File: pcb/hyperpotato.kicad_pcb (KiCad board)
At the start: 2 copper layers, 119.4 x 94.3 mm, 13 parts, among them SW1 SW_Push_45deg, SW10 SW_Push_45deg, SW11 SW_Push_45deg, SW12 SW_Push_45deg, SW13 SW_Push_45deg, SW2 SW_Push_45deg, SW3 SW_Push_45deg, SW4 SW_Push_45deg, SW5 SW_Push_45deg, SW6 SW_Push_45deg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

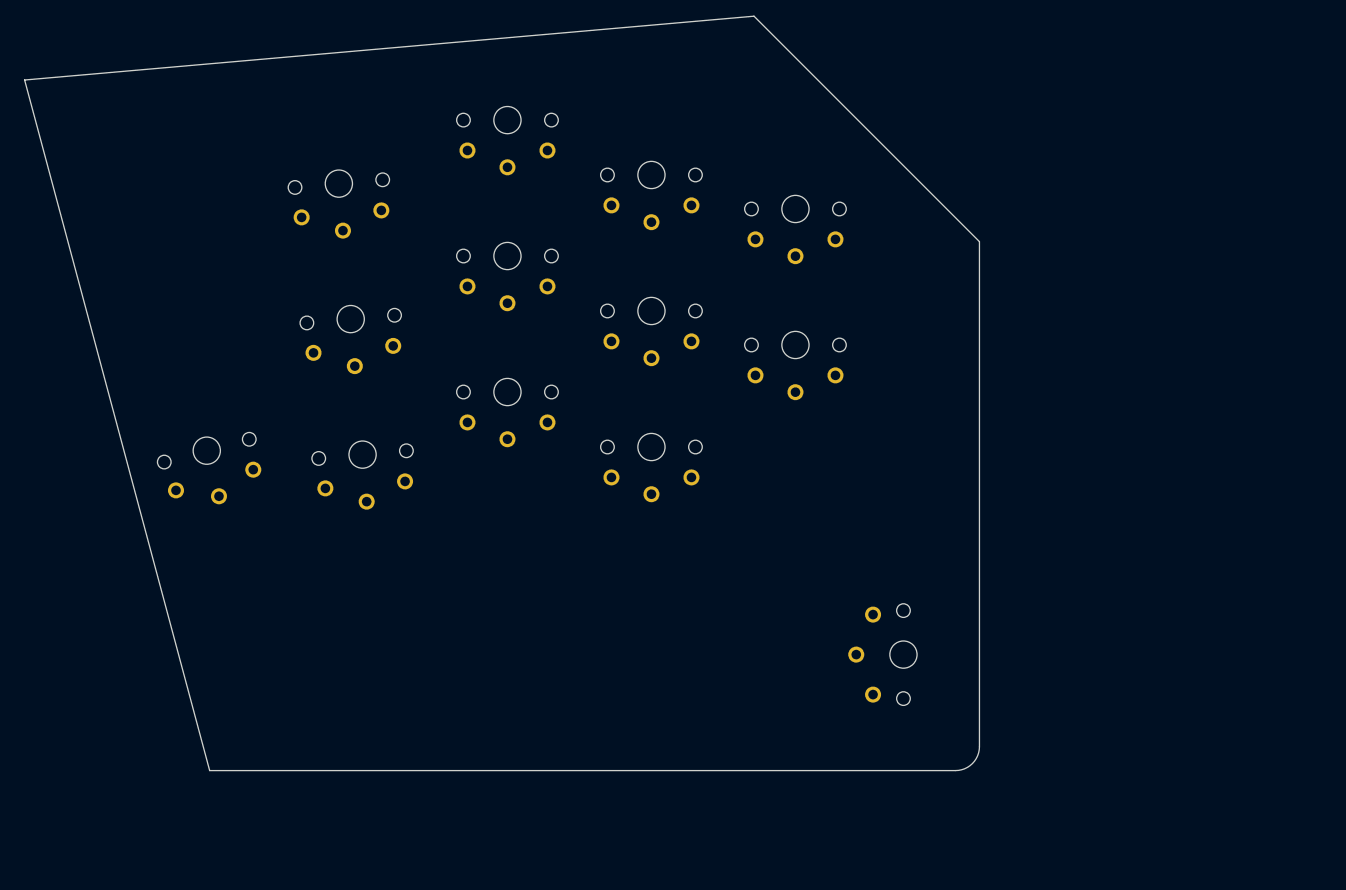
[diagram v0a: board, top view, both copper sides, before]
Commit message: Add pcb outline
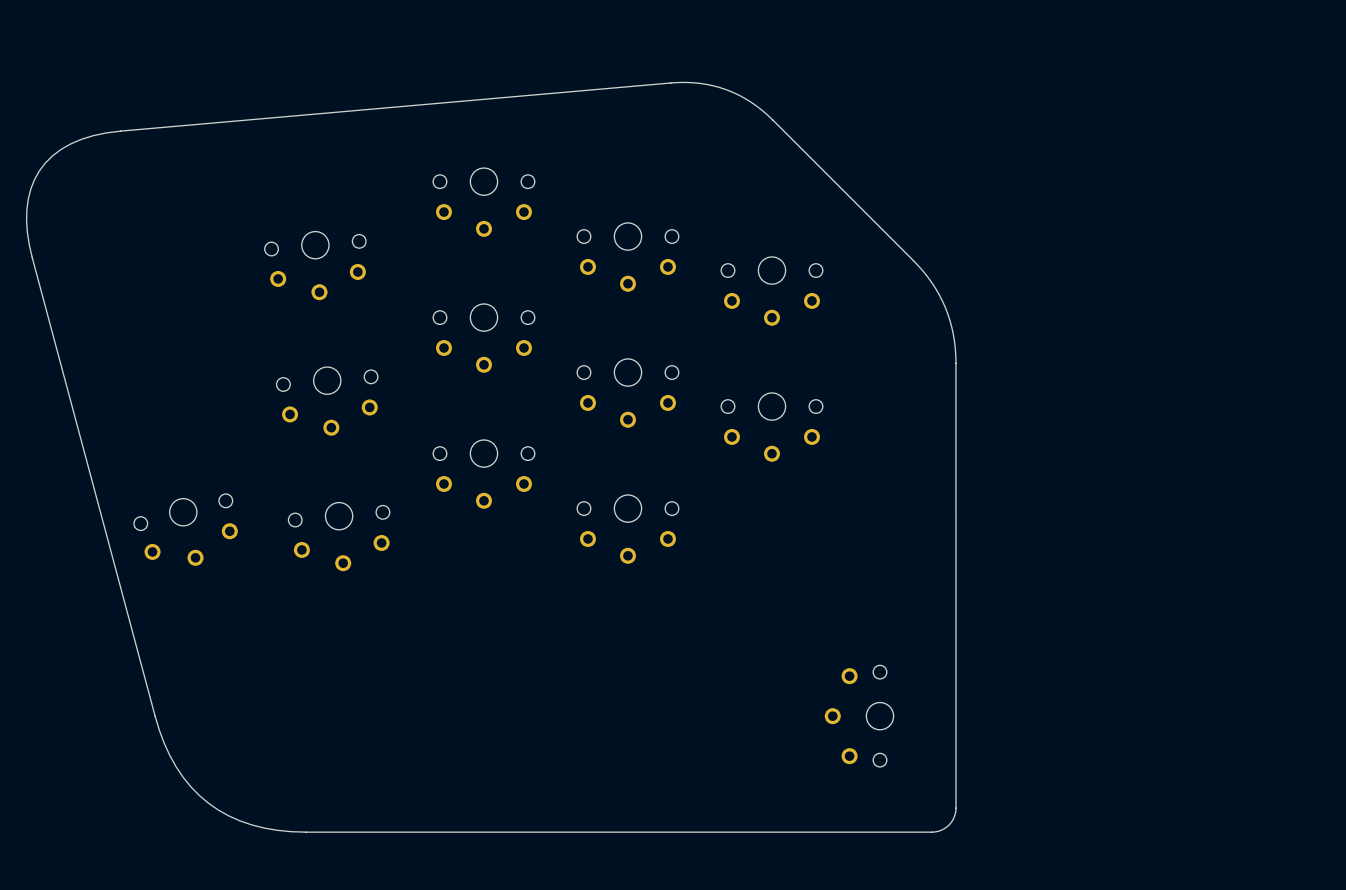
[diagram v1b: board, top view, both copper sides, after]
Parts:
- moved SW9 8.24 mm to (132.6, 91.7)
- moved SW12 8.24 mm to (114.6, 104.5)
- moved SW1 8.24 mm to (75.5, 71.5)
- moved SW10 8.24 mm to (78.4, 105.4)
- moved SW7 8.24 mm to (96.6, 80.6)
- moved SW2 8.24 mm to (96.6, 63.6)
- moved SW13 8.24 mm to (146.1, 130.4)
- moved SW11 8.24 mm to (96.6, 97.6)
- moved SW6 8.24 mm to (77.0, 88.5)
- moved SW4 8.24 mm to (132.6, 74.7)
- moved SW5 8.24 mm to (59.0, 104.9)
- moved SW8 8.24 mm to (114.6, 87.5)
- moved SW3 8.24 mm to (114.6, 70.5)
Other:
- board size 119.4 x 94.3 mm -> 116.2 x 93.7 mm
- board text added: "15mm offset"
- board text added: "3mm offset"
- board text added: "7.5mm offset"

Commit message: Place test xiao footprint
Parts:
- added REF**: Xiao_nRF52840_ACH_1, PCM_marbastlib-xp-promicroish:Xiao_nRF52840_AC_Reflow, F.Cu at (57.3, 64.5)
- moved SW13 5.52 mm to (143.1, 135.1), turned to -95 degrees
- moved SW4 4.20 mm to (134.5, 78.4), turned to -5 degrees
- moved SW9 3.68 mm to (133.0, 95.4), turned to -5 degrees
- moved SW3 3.23 mm to (117.0, 72.6), turned to -5 degrees
- moved SW2 3.13 mm to (99.6, 64.2), turned to -5 degrees
- moved SW5 2.84 mm to (58.6, 102.1), turned to 10 degrees
- moved SW1 2.76 mm to (77.9, 70.3), turned to 0 degrees
- moved SW8 2.29 mm to (115.5, 89.6), turned to -5 degrees
- moved SW12 2.10 mm to (114.0, 106.5), turned to -5 degrees
- moved SW7 1.68 mm to (98.2, 81.2), turned to -5 degrees
- moved SW6 1.54 mm to (77.9, 87.3), turned to 0 degrees
- moved SW10 1.23 mm to (77.9, 104.3), turned to 0 degrees
- moved SW11 0.50 mm to (96.7, 98.1), turned to -5 degrees
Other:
- board size 116.2 x 93.7 mm -> 114.3 x 96.1 mm

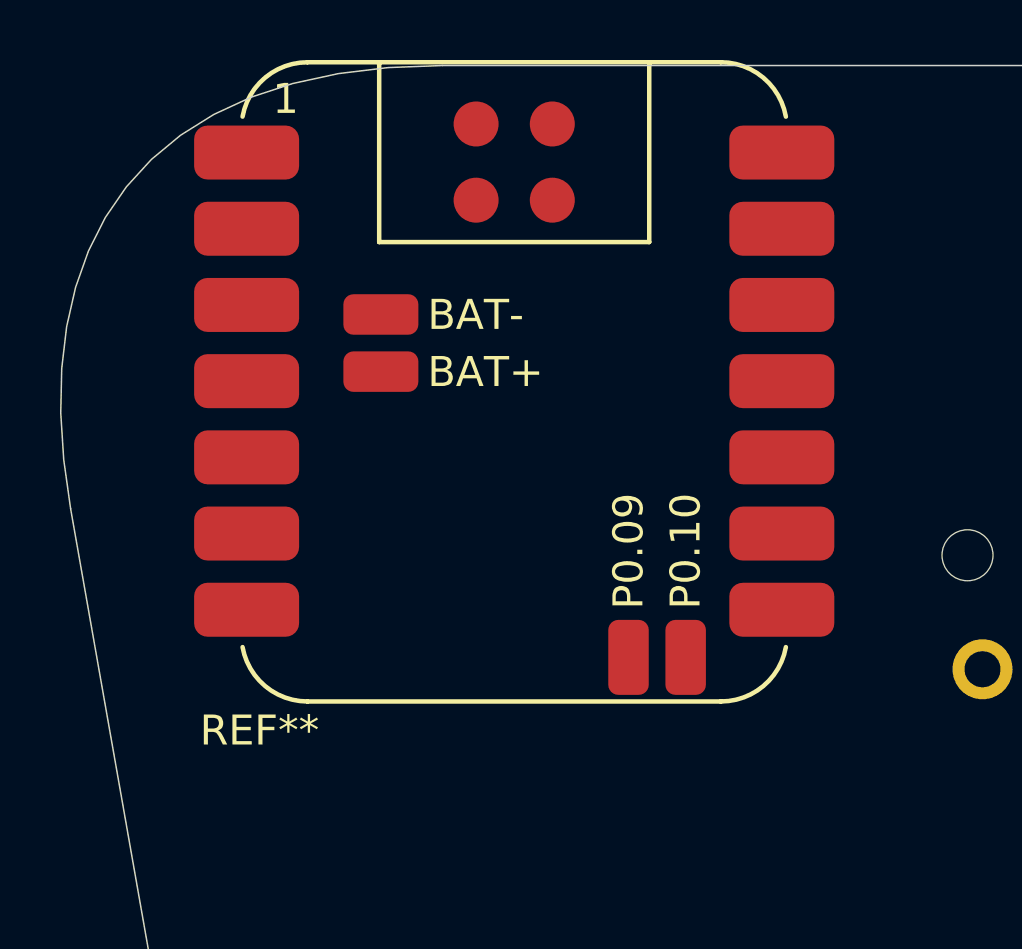
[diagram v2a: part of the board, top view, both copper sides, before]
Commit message: Remove pullup resistors and reset circuit
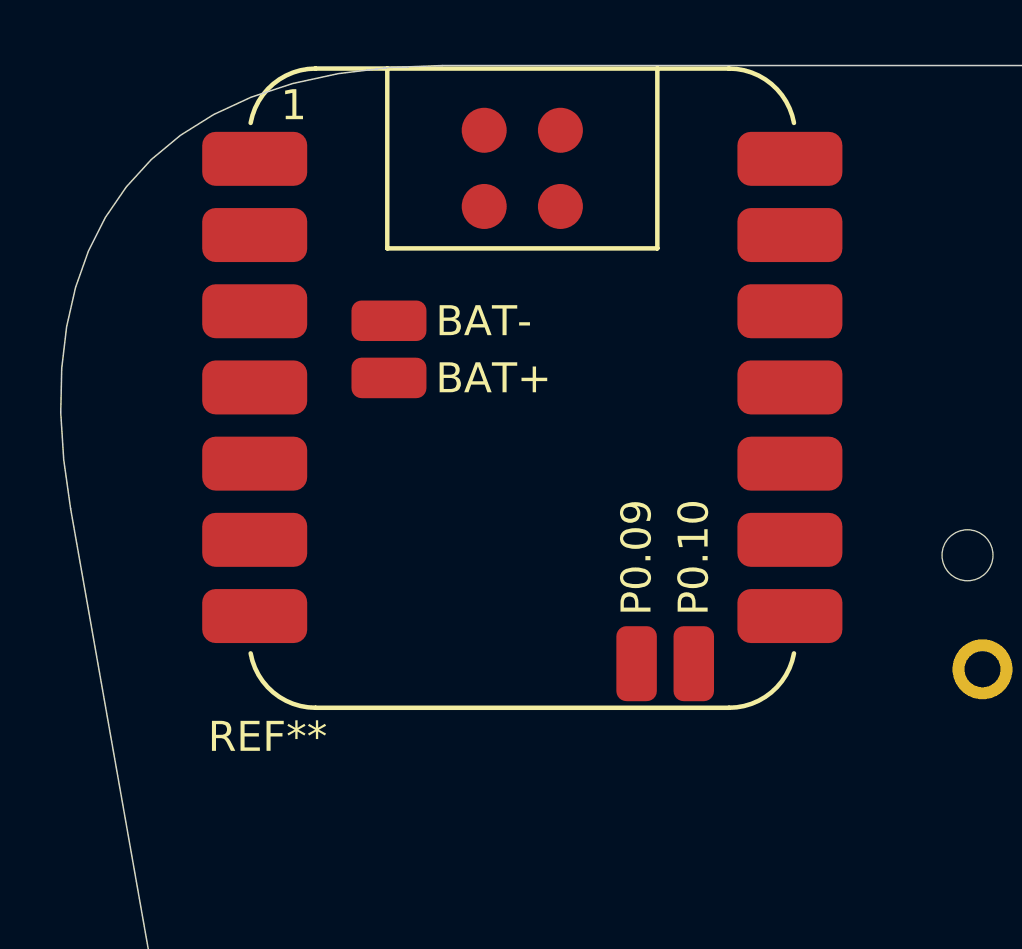
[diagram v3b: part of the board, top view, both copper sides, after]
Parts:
- moved REF** 0.34 mm to (57.6, 64.7)
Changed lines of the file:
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@@
 		)
 		(pad "1" thru_hole circle
-			(at 4.999999 3.799999 175)
+			(at 4.999999 3.799998 175)
 			(size 2 2)
 			(drill 1.2)
@@
 		)
 		(pad "1" thru_hole circle
-			(at 4.999999 3.799999 175)
+			(at 4.999999 3.799998 175)
 			(size 2 2)
 			(drill 1.2)
@@
 		)
 		(pad "1" thru_hole circle
-			(at 4.999999 3.799999 175)
+			(at 4.999999 3.799998 175)
 			(size 2 2)
 			(drill 1.2)
@@
 		(fp_arc
 			(start -6.949999 -6.450002)
-			(mid -6.80355 -6.803554)
+			(mid -6.803551 -6.803553)
 			(end -6.449998 -6.949998)
 			(stroke
@@
 		(fp_arc
 			(start -6.450002 6.949999)
-			(mid -6.803554 6.80355)
+			(mid -6.803553 6.803551)
 			(end -6.949998 6.449998)
 			(stroke
@@
 		)
 		(pad "1" thru_hole circle
-			(at 4.999999 3.799999 175)
+			(at 4.999999 3.799998 175)
 			(size 2 2)
 			(drill 1.2)
@@
 		(fp_arc
 			(start -6.949999 -6.450002)
-			(mid -6.80355 -6.803554)
+			(mid -6.803551 -6.803553)
 			(end -6.449998 -6.949998)
 			(stroke
@@
 		(fp_arc
 			(start -6.450002 6.949999)
-			(mid -6.803554 6.80355)
+			(mid -6.803553 6.803551)
 			(end -6.949998 6.449998)
 			(stroke
@@
 		)
 		(pad "1" thru_hole circle
-			(at 4.999999 3.799999 175)
+			(at 4.999999 3.799998 175)
 			(size 2 2)
 			(drill 1.2)
@@
 		)
 		(pad "1" thru_hole circle
-			(at 4.999999 3.799999 175)
+			(at 4.999999 3.799998 175)
 			(size 2 2)
 			(drill 1.2)
@@
 		(fp_arc
 			(start 6.449999 -6.949996)
-			(mid 6.803553 -6.803552)
+			(mid 6.80355 -6.803551)
 			(end 6.95 -6.45)
 			(stroke
@@
 		(fp_arc
 			(start 6.949996 6.449999)
-			(mid 6.803552 6.803553)
+			(mid 6.803551 6.80355)
 			(end 6.45 6.95)
 			(stroke
@@
 		)
 		(pad "1" thru_hole circle
-			(at 4.999999 3.799999 175)
+			(at 4.999999 3.799998 175)
 			(size 2 2)
 			(drill 1.2)
@@
 		(fp_arc
 			(start -6.949999 -6.450002)
-			(mid -6.80355 -6.803554)
+			(mid -6.803551 -6.803553)
 			(end -6.449998 -6.949998)
 			(stroke
@@
 		(fp_arc
 			(start -6.450002 6.949999)
-			(mid -6.803554 6.80355)
+			(mid -6.803553 6.803551)
 			(end -6.949998 6.449998)
 			(stroke
@@
 		)
 		(pad "1" thru_hole circle
-			(at 4.999999 3.799999 85)
+			(at 4.999999 3.799998 85)
 			(size 2 2)
 			(drill 1.2)
@@
 		)
 		(pad "1" thru_hole circle
-			(at 4.999999 3.799999 175)
+			(at 4.999999 3.799998 175)
 			(size 2 2)
 			(drill 1.2)
@@
 	(footprint "PCM_marbastlib-xp-promicroish:Xiao_nRF52840_AC_Reflow"
 		(layer "F.Cu")
-		(at 57.334997 64.493698)
+		(at 57.604997 64.703698)
 		(descr "Footprint for Elite-C controllers, through hole and castellated pads")
 		(property "Reference" "REF**"

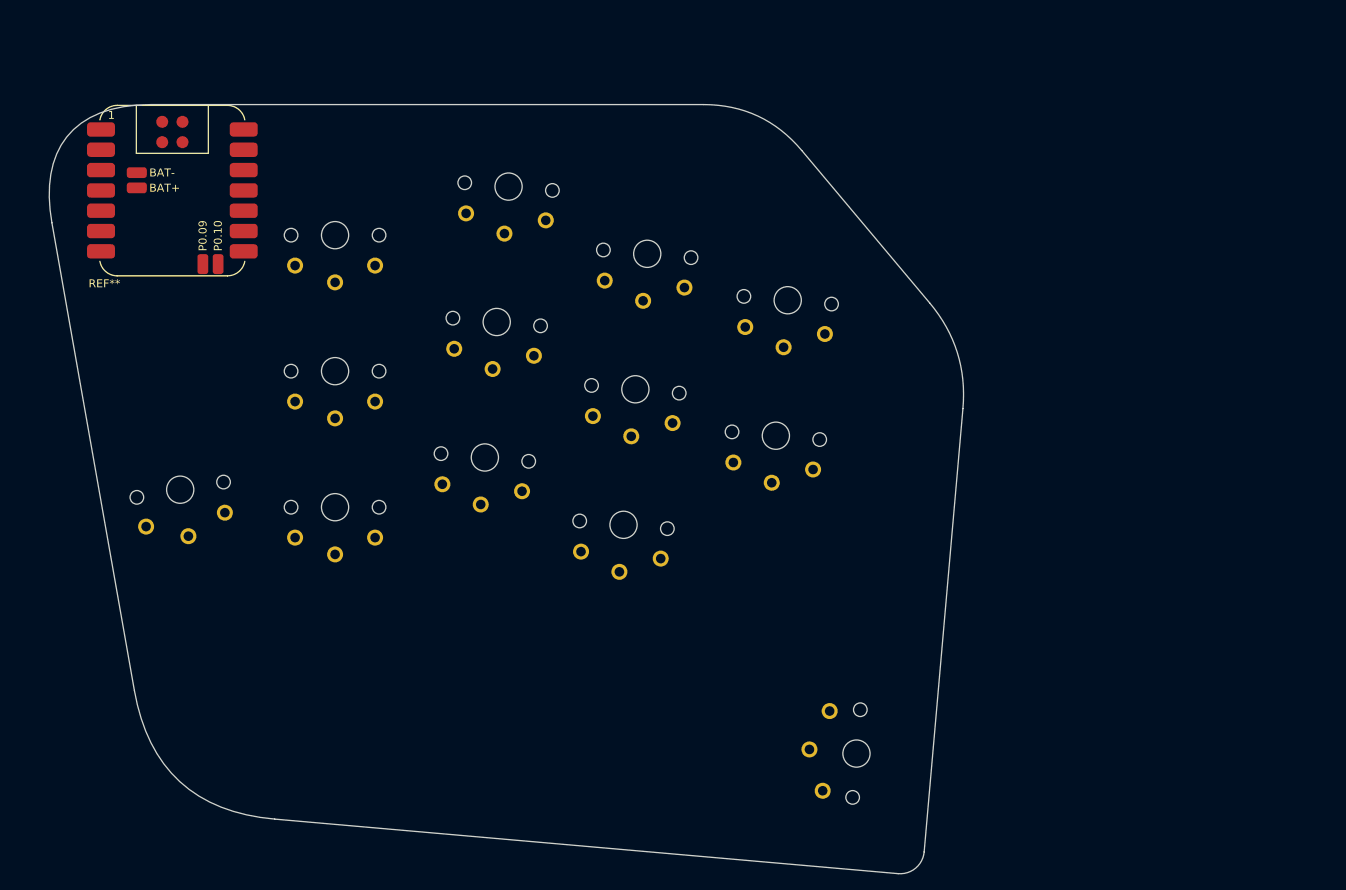
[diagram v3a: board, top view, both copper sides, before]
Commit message: Adjust main components placement
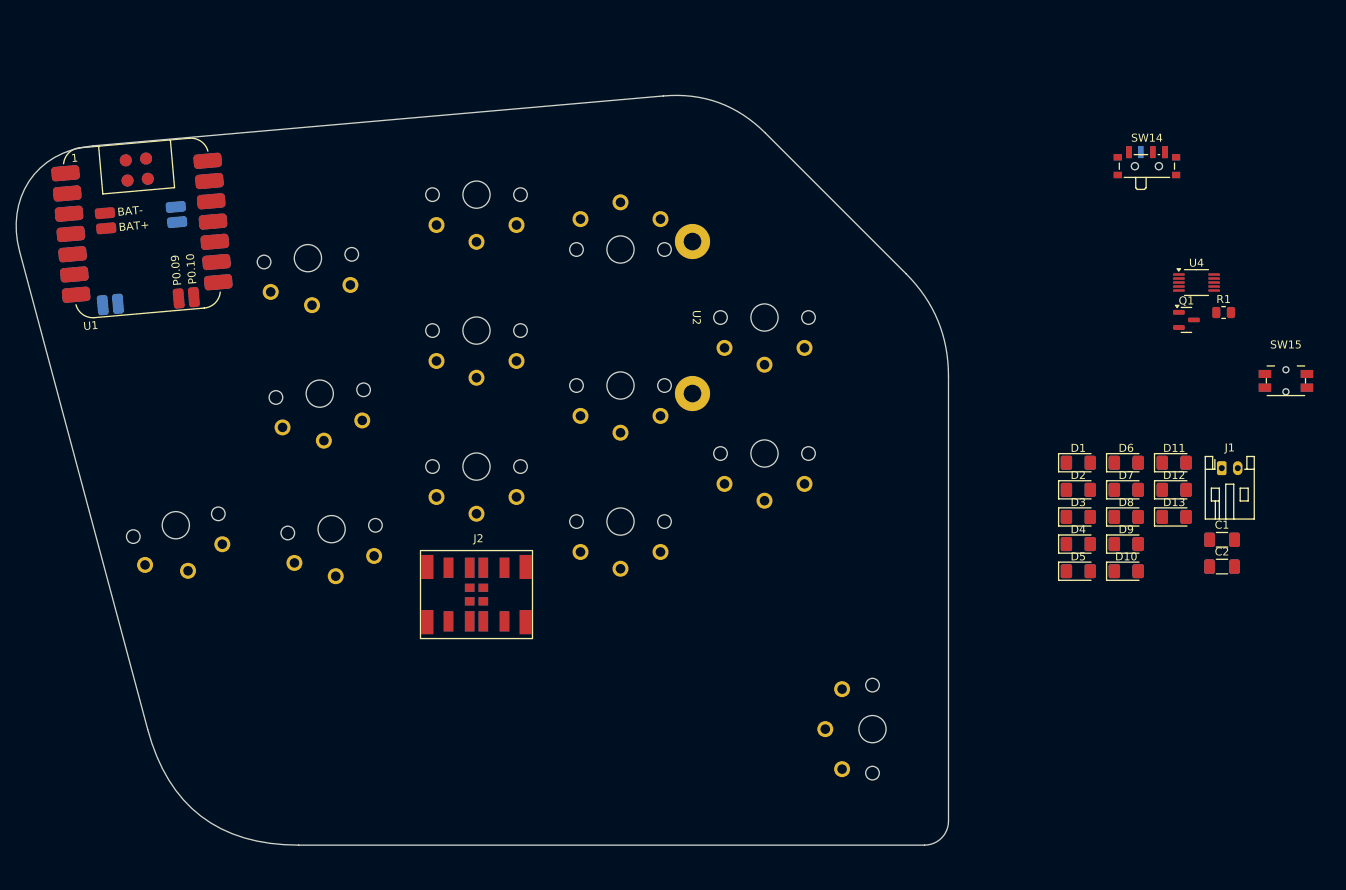
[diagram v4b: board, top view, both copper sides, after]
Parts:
- added C1: 1uF, ssbb_parts:C_1206_HandSolder_reversible, F.Cu at (188.8, 108.4)
- added C2: 1uF, ssbb_parts:C_1206_HandSolder_reversible, F.Cu at (188.8, 111.7)
- added D1: D_Small, ssbb_parts:D_1206_HandSolder_reversible, F.Cu at (170.8, 98.7)
- added D10: D_Small, ssbb_parts:D_1206_HandSolder_reversible, F.Cu at (176.8, 112.3)
- added D11: D_Small, ssbb_parts:D_1206_HandSolder_reversible, F.Cu at (182.8, 98.7)
- added D12: D_Small, ssbb_parts:D_1206_HandSolder_reversible, F.Cu at (182.8, 102.1)
- added D13: D_Small, ssbb_parts:D_1206_HandSolder_reversible, F.Cu at (182.8, 105.5)
- added D2: D_Small, ssbb_parts:D_1206_HandSolder_reversible, F.Cu at (170.8, 102.1)
- added D3: D_Small, ssbb_parts:D_1206_HandSolder_reversible, F.Cu at (170.8, 105.5)
- added D4: D_Small, ssbb_parts:D_1206_HandSolder_reversible, F.Cu at (170.8, 108.9)
- added D5: D_Small, ssbb_parts:D_1206_HandSolder_reversible, F.Cu at (170.8, 112.3)
- added D6: D_Small, ssbb_parts:D_1206_HandSolder_reversible, F.Cu at (176.8, 98.7)
- added D7: D_Small, ssbb_parts:D_1206_HandSolder_reversible, F.Cu at (176.8, 102.1)
- added D8: D_Small, ssbb_parts:D_1206_HandSolder_reversible, F.Cu at (176.8, 105.5)
- added D9: D_Small, ssbb_parts:D_1206_HandSolder_reversible, F.Cu at (176.8, 108.9)
- added J1: Conn_01x02_Socket, ssbb_parts:JST_PH_S2B-PH-K_Horizontal_reversible, F.Cu at (188.8, 99.4)
- added J2: Conn_01x03_Pin, ssbb_parts:ELV1411A_reversible, F.Cu at (95.6, 115.2)
- added Q1: AO3401A, Package_TO_SOT_SMD:SOT-23, F.Cu at (184.4, 80.9)
- added R1: 2M, Resistor_SMD:R_0805_2012Metric, F.Cu at (189.0, 80.0)
- added SW14: SW_SPDT, ssbb_parts:SW_SPDT_PCM12_reversible, F.Cu at (179.4, 61.3)
- added SW15: SW_Push, ssbb_parts:Panasonic_EVQPUL_EVQPUC_reversible, F.Cu at (196.8, 88.5)
- added U2: SK8707-01-SENSOR, ssbb_parts:Sprintek_SK8707-01_Sensor, F.Cu at (122.6, 80.6)
- added U4: DRV2605LDGS, Package_SO:VSSOP-10_3x3mm_P0.5mm, F.Cu at (185.6, 76.2)
- U1: renamed from REF**; value Xiao_nRF52840_ACH_1 -> Seeeduino Xiao nRF52840; footprint PCM_marbastlib-xp-promicroish:Xiao_nRF52840_AC_Reflow -> ssbb_parts:Xiao_nRF52840_AC_Reflow_reversible
- moved U1 6.02 mm to (53.8, 69.4), turned to 5 degrees
- moved SW5 4.47 mm to (58.0, 106.6), turned to 15 degrees
- moved SW1 4.45 mm to (74.5, 73.2), turned to 5 degrees
- moved SW2 4.13 mm to (95.6, 65.2), turned to 0 degrees
- moved SW13 3.65 mm to (145.1, 132.0), turned to -90 degrees
- moved SW4 3.62 mm to (131.6, 80.6), turned to 0 degrees
- moved SW6 3.40 mm to (76.0, 90.1), turned to 5 degrees
- moved SW3 3.38 mm to (113.6, 72.1), turned to 180 degrees
- moved SW10 2.78 mm to (77.5, 107.0), turned to 5 degrees
- moved SW7 2.74 mm to (95.6, 82.2), turned to 0 degrees
- moved SW9 2.64 mm to (131.6, 97.6), turned to 0 degrees
- moved SW8 1.92 mm to (113.6, 89.1), turned to 0 degrees
- moved SW11 1.54 mm to (95.6, 99.2), turned to 0 degrees
- moved SW12 0.55 mm to (113.6, 106.1), turned to 0 degrees
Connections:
- U1 pad 1: (no net) -> unconnected-(U1-P0.02-Pad1)
- U1 pad 10: (no net) -> +3.3V
- U1 pad 11: (no net) -> unconnected-(U1-P1.15-Pad11)
- U1 pad 12: (no net) -> unconnected-(U1-P1.14-Pad12)
- U1 pad 13: (no net) -> unconnected-(U1-P1.13-Pad13)
- U1 pad 14: (no net) -> unconnected-(U1-P1.12-Pad14)
- U1 pad 15: (no net) -> GND
- U1 pad 16: (no net) -> BAT+
- U1 pad 17: (no net) -> unconnected-(U1-P0.09-Pad17)
- U1 pad 18: (no net) -> unconnected-(U1-P0.10-Pad18)
- U1 pad 19: (no net) -> unconnected-(U1-DIO-Pad19)
- U1 pad 2: (no net) -> unconnected-(U1-P0.03-Pad2)
- U1 pad 20: (no net) -> unconnected-(U1-CLK-Pad20)_1
- U1 pad 21: (no net) -> RESET
- U1 pad 22: (no net) -> GND
- U1 pad 3: (no net) -> unconnected-(U1-P0.28-Pad3)
- U1 pad 4: (no net) -> unconnected-(U1-P0.29-Pad4)
- U1 pad 5: (no net) -> unconnected-(U1-P0.04-Pad5)
- U1 pad 6: (no net) -> unconnected-(U1-P0.05-Pad6)
- U1 pad 7: (no net) -> unconnected-(U1-P1.11-Pad7)
- U1 pad 8: (no net) -> unconnected-(U1-5V-Pad8)
- U1 pad 9: (no net) -> GND
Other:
- board size 114.3 x 96.1 mm -> 116.5 x 93.7 mm
- board text added: "12.5mm offset"
- board text added: "MHP50 Reflow Plate"
- board text added: "Trackpoint is going to be mounted on the right side, and the switch pin won't collide with it in this orientation. Will need to cut stab pin though."
